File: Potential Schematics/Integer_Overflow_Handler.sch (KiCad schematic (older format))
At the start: 10 parts

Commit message: Made the registers
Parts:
- gave numbers to parts that had none: 7
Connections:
- net CoutALU: now also U35.4; no longer U35.1
- net OP0: now also U10.11; no longer U10.1
- net OP1: now also U10.5; no longer U10.1
- net OP3: now also U10.3; no longer U10.1
- net RS_Latch/R: now also U35.6; no longer U35.3
- net at U21.2: now also U10.4; no longer U10.2
- net at U21.3: now also U21.13; no longer U21.2
- net at U5.1: now also U10.10; no longer U10.2
- net at U5.2: now also U10.6; no longer U10.2
- net at U5.3: now also U21.12; no longer U21.1
- new net: U21.11, U35.5
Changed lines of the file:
@@
 $Descr A4 11693 8268
 encoding utf-8
-Sheet 21 22
+Sheet 21 449
 Title "Integer Overflow Handler"
-Date ""
-Rev ""
+Date "2018-09-14"
+Rev "1"
 Comp ""
 Comment1 ""
@@
 CoutALU
 $Comp
-L 74LS08 U?
+L 74LS08 U21
 U 1 1 5B9D62F2
 P 3600 3400
-F 0 "U?" H 3600 3450 50  0000 C CNN
+F 0 "U21" H 3600 3450 50  0000 C CNN
 F 1 "74LS08" H 3600 3350 50  0000 C CNN
 F 2 "" H 3600 3400 50  0001 C CNN
@@
 $EndComp
 $Comp
-L 74LS08 U?
+L 74LS08 U5
 U 1 1 5B9D634D
 P 3600 2900
-F 0 "U?" H 3600 2950 50  0000 C CNN
+F 0 "U5" H 3600 2950 50  0000 C CNN
 F 1 "74LS08" H 3600 2850 50  0000 C CNN
 F 2 "" H 3600 2900 50  0001 C CNN
@@
 $EndComp
 $Comp
-L 74LS08 U?
-U 1 1 5B9D6375
+L 74LS08 U35
+U 2 1 5B9D6375
 P 6450 3900
-F 0 "U?" H 6450 3950 50  0000 C CNN
+F 0 "U35" H 6450 3950 50  0000 C CNN
 F 1 "74LS08" H 6450 3850 50  0000 C CNN
 F 2 "" H 6450 3900 50  0001 C CNN
 F 3 "" H 6450 3900 50  0001 C CNN
-	1    6450 3900
+	2    6450 3900
 	0    1    1    0
 $EndComp
 $Comp
-L 74LS08 U?
-U 1 1 5B9D643C
+L 74LS08 U21
+U 4 1 5B9D643C
 P 5050 3150
-F 0 "U?" H 5050 3200 50  0000 C CNN
+F 0 "U21" H 5050 3200 50  0000 C CNN
 F 1 "74LS08" H 5050 3100 50  0000 C CNN
 F 2 "" H 5050 3150 50  0001 C CNN
 F 3 "" H 5050 3150 50  0001 C CNN
-	1    5050 3150
+	4    5050 3150
 	1    0    0    -1
 $EndComp
@@
 	2200 3300 3000 3300
 $Comp
-L 74LS04 U?
-U 1 1 5B9D64D7
+L 74LS04 U10
+U 5 1 5B9D64D7
 P 2550 2450
-F 0 "U?" H 2745 2565 50  0000 C CNN
+F 0 "U10" H 2745 2565 50  0000 C CNN
 F 1 "74LS04" H 2740 2325 50  0000 C CNN
 F 2 "" H 2550 2450 50  0001 C CNN
 F 3 "" H 2550 2450 50  0001 C CNN
-	1    2550 2450
+	5    2550 2450
 	1    0    0    -1
 $EndComp
 $Comp
-L 74LS04 U?
-U 1 1 5B9D652D
+L 74LS04 U10
+U 3 1 5B9D652D
 P 2400 2750
-F 0 "U?" H 2595 2865 50  0000 C CNN
+F 0 "U10" H 2595 2865 50  0000 C CNN
 F 1 "74LS04" H 2590 2625 50  0000 C CNN
 F 2 "" H 2400 2750 50  0001 C CNN
 F 3 "" H 2400 2750 50  0001 C CNN
-	1    2400 2750
+	3    2400 2750
 	1    0    0    -1
 $EndComp
 $Comp
-L 74LS04 U?
-U 1 1 5B9D6565
+L 74LS04 U10
+U 2 1 5B9D6565
 P 1950 3400
-F 0 "U?" H 2145 3515 50  0000 C CNN
+F 0 "U10" H 2145 3515 50  0000 C CNN
 F 1 "74LS04" H 2140 3275 50  0000 C CNN
 F 2 "" H 1950 3400 50  0001 C CNN
 F 3 "" H 1950 3400 50  0001 C CNN
-	1    1950 3400
+	2    1950 3400
 	0    1    1    0
 $EndComp
@@
 	1950 2450 2100 2450
 $Comp
-L LED D?
+L LED D1
 U 1 1 5B9D6685
 P 8100 4700
-F 0 "D?" H 8100 4800 50  0000 C CNN
+F 0 "D1" H 8100 4800 50  0000 C CNN
 F 1 "LED" H 8100 4600 50  0000 C CNN
 F 2 "" H 8100 4700 50  0001 C CNN
@@
 $EndComp
 $Comp
-L R R?
+L R R1
 U 1 1 5B9D6786
 P 8400 4700
-F 0 "R?" V 8480 4700 50  0000 C CNN
+F 0 "R1" V 8480 4700 50  0000 C CNN
 F 1 "R" V 8400 4700 50  0000 C CNN
 F 2 "" V 8330 4700 50  0001 C CNN
@@
 $EndComp
 $Comp
-L GND #PWR?
+L GND #PWR1
 U 1 1 5B9D67B7
 P 8550 4700
-F 0 "#PWR?" H 8550 4450 50  0001 C CNN
+F 0 "#PWR1" H 8550 4450 50  0001 C CNN
 F 1 "GND" H 8550 4550 50  0000 C CNN
 F 2 "" H 8550 4700 50  0001 C CNN
@@
 $EndSheet
 $Comp
-L SW_Push SW?
+L SW_Push SW1
 U 1 1 5B9D789D
 P 5150 4700
-F 0 "SW?" H 5200 4800 50  0000 L CNN
+F 0 "SW1" H 5200 4800 50  0000 L CNN
 F 1 "SW_Push" H 5150 4640 50  0000 C CNN
 F 2 "" H 5150 4900 50  0001 C CNN

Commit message: Adding Multiply Devide
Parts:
- D1: symbol LED -> Device:LED
- R1: symbol R -> Device:R
- SW1: symbol SW_Push -> 4-bit_processor-rescue:SW_Push
- U10: symbol 74LS04 -> 4-bit_processor-rescue:74LS04
- U21, U35, U5: symbol 74LS08 -> 4-bit_processor-rescue:74LS08
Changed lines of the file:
@@
-EESchema Schematic File Version 2
-LIBS:power
-LIBS:device
-LIBS:switches
-LIBS:relays
-LIBS:motors
-LIBS:transistors
-LIBS:conn
-LIBS:linear
-LIBS:regul
-LIBS:74xx
-LIBS:cmos4000
-LIBS:adc-dac
-LIBS:memory
-LIBS:xilinx
-LIBS:microcontrollers
-LIBS:dsp
-LIBS:microchip
-LIBS:analog_switches
-LIBS:motorola
-LIBS:texas
-LIBS:intel
-LIBS:audio
-LIBS:interface
-LIBS:digital-audio
-LIBS:philips
-LIBS:display
-LIBS:cypress
-LIBS:siliconi
-LIBS:opto
-LIBS:atmel
-LIBS:contrib
-LIBS:valves
+EESchema Schematic File Version 4
 LIBS:4-bit_processor-cache
-EELAYER 25 0
+EELAYER 26 0
 EELAYER END
 $Descr A4 11693 8268
 encoding utf-8
-Sheet 21 449
+Sheet 21 451
 Title "Integer Overflow Handler"
 Date "2018-09-14"
@@
 CoutALU
 $Comp
-L 74LS08 U21
+L 4-bit_processor-rescue:74LS08 U21
 U 1 1 5B9D62F2
 P 3600 3400
@@
 $EndComp
 $Comp
-L 74LS08 U5
+L 4-bit_processor-rescue:74LS08 U5
 U 1 1 5B9D634D
 P 3600 2900
@@
 $EndComp
 $Comp
-L 74LS08 U35
+L 4-bit_processor-rescue:74LS08 U35
 U 2 1 5B9D6375
 P 6450 3900
@@
 $EndComp
 $Comp
-L 74LS08 U21
+L 4-bit_processor-rescue:74LS08 U21
 U 4 1 5B9D643C
 P 5050 3150
@@
 	2200 3300 3000 3300
 $Comp
-L 74LS04 U10
+L 4-bit_processor-rescue:74LS04 U10
 U 5 1 5B9D64D7
 P 2550 2450
@@
 $EndComp
 $Comp
-L 74LS04 U10
+L 4-bit_processor-rescue:74LS04 U10
 U 3 1 5B9D652D
 P 2400 2750
@@
 $EndComp
 $Comp
-L 74LS04 U10
+L 4-bit_processor-rescue:74LS04 U10
 U 2 1 5B9D6565
 P 1950 3400
@@
 	1950 2450 2100 2450
 $Comp
-L LED D1
+L Device:LED D1
 U 1 1 5B9D6685
 P 8100 4700
@@
 $EndComp
 $Comp
-L R R1
+L Device:R R1
 U 1 1 5B9D6786
 P 8400 4700
@@
 $EndComp
 $Comp
-L GND #PWR1
+L power:GND #PWR1
 U 1 1 5B9D67B7
 P 8550 4700
@@
 $EndSheet
 $Comp
-L SW_Push SW1
+L 4-bit_processor-rescue:SW_Push SW1
 U 1 1 5B9D789D
 P 5150 4700

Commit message: Finished PCB
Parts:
- D1: footprint (none) -> LEDs:LED_D1.8mm_W1.8mm_H2.4mm_Horizontal_O3.81mm_Z4.9mm
- R1: footprint (none) -> Resistors_THT:R_Axial_DIN0922_L20.0mm_D9.0mm_P30.48mm_Horizontal
- SW1: footprint (none) -> Buttons_Switches_THT:SW_DIP_x2_W7.62mm_Slide_LowProfile
- U25: renamed from U10; footprint (none) -> Daniel_Kopp:DIP-14_300_ELL
- U26, U28: renamed from U21; footprint (none) -> Daniel_Kopp:DIP-14_300_ELL
- U26: renamed from U5; footprint (none) -> Daniel_Kopp:DIP-14_300_ELL
- U28: renamed from U35; footprint (none) -> Daniel_Kopp:DIP-14_300_ELL
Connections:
- net OP0: now also U25.9; no longer U25.11
- net OP2: now also U26.12; no longer U26.1
- net at U25.4: now also U26.13; no longer U26.2
- net at U25.6: now also U26.10; no longer U26.2
- net at U28.5: now also U28.3; no longer U28.11
- new net: U26.11, U28.2
- new net: U26.8, U28.1
- new net: U25.8, U26.9
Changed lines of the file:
@@
 $Descr A4 11693 8268
 encoding utf-8
-Sheet 21 451
+Sheet 21 456
 Title "Integer Overflow Handler"
 Date "2018-09-14"
@@
 CoutALU
 $Comp
-L 4-bit_processor-rescue:74LS08 U21
-U 1 1 5B9D62F2
+L 4-bit_processor-rescue:74LS08 U26
+U 4 1 5B9D62F2
 P 3600 3400
-F 0 "U21" H 3600 3450 50  0000 C CNN
+F 0 "U26" H 3600 3450 50  0000 C CNN
 F 1 "74LS08" H 3600 3350 50  0000 C CNN
-F 2 "" H 3600 3400 50  0001 C CNN
+F 2 "Daniel_Kopp:DIP-14_300_ELL" H 3600 3400 50  0001 C CNN
 F 3 "" H 3600 3400 50  0001 C CNN
-	1    3600 3400
+	4    3600 3400
 	1    0    0    -1
 $EndComp
 $Comp
-L 4-bit_processor-rescue:74LS08 U5
-U 1 1 5B9D634D
+L 4-bit_processor-rescue:74LS08 U26
+U 3 1 5B9D634D
 P 3600 2900
-F 0 "U5" H 3600 2950 50  0000 C CNN
+F 0 "U26" H 3600 2950 50  0000 C CNN
 F 1 "74LS08" H 3600 2850 50  0000 C CNN
-F 2 "" H 3600 2900 50  0001 C CNN
+F 2 "Daniel_Kopp:DIP-14_300_ELL" H 3600 2900 50  0001 C CNN
 F 3 "" H 3600 2900 50  0001 C CNN
-	1    3600 2900
+	3    3600 2900
 	1    0    0    -1
 $EndComp
 $Comp
-L 4-bit_processor-rescue:74LS08 U35
+L 4-bit_processor-rescue:74LS08 U28
 U 2 1 5B9D6375
 P 6450 3900
-F 0 "U35" H 6450 3950 50  0000 C CNN
+F 0 "U28" H 6450 3950 50  0000 C CNN
 F 1 "74LS08" H 6450 3850 50  0000 C CNN
-F 2 "" H 6450 3900 50  0001 C CNN
+F 2 "Daniel_Kopp:DIP-14_300_ELL" H 6450 3900 50  0001 C CNN
 F 3 "" H 6450 3900 50  0001 C CNN
 	2    6450 3900
@@
 $EndComp
 $Comp
-L 4-bit_processor-rescue:74LS08 U21
-U 4 1 5B9D643C
+L 4-bit_processor-rescue:74LS08 U28
+U 1 1 5B9D643C
 P 5050 3150
-F 0 "U21" H 5050 3200 50  0000 C CNN
+F 0 "U28" H 5050 3200 50  0000 C CNN
 F 1 "74LS08" H 5050 3100 50  0000 C CNN
-F 2 "" H 5050 3150 50  0001 C CNN
+F 2 "Daniel_Kopp:DIP-14_300_ELL" H 5050 3150 50  0001 C CNN
 F 3 "" H 5050 3150 50  0001 C CNN
-	4    5050 3150
+	1    5050 3150
 	1    0    0    -1
 $EndComp
@@
 	2200 3300 3000 3300
 $Comp
-L 4-bit_processor-rescue:74LS04 U10
-U 5 1 5B9D64D7
+L 4-bit_processor-rescue:74LS04 U25
+U 4 1 5B9D64D7
 P 2550 2450
-F 0 "U10" H 2745 2565 50  0000 C CNN
+F 0 "U25" H 2745 2565 50  0000 C CNN
 F 1 "74LS04" H 2740 2325 50  0000 C CNN
-F 2 "" H 2550 2450 50  0001 C CNN
+F 2 "Daniel_Kopp:DIP-14_300_ELL" H 2550 2450 50  0001 C CNN
 F 3 "" H 2550 2450 50  0001 C CNN
-	5    2550 2450
+	4    2550 2450
 	1    0    0    -1
 $EndComp
 $Comp
-L 4-bit_processor-rescue:74LS04 U10
+L 4-bit_processor-rescue:74LS04 U25
 U 3 1 5B9D652D
 P 2400 2750
-F 0 "U10" H 2595 2865 50  0000 C CNN
+F 0 "U25" H 2595 2865 50  0000 C CNN
 F 1 "74LS04" H 2590 2625 50  0000 C CNN
-F 2 "" H 2400 2750 50  0001 C CNN
+F 2 "Daniel_Kopp:DIP-14_300_ELL" H 2400 2750 50  0001 C CNN
 F 3 "" H 2400 2750 50  0001 C CNN
 	3    2400 2750
@@
 $EndComp
 $Comp
-L 4-bit_processor-rescue:74LS04 U10
+L 4-bit_processor-rescue:74LS04 U25
 U 2 1 5B9D6565
 P 1950 3400
-F 0 "U10" H 2145 3515 50  0000 C CNN
+F 0 "U25" H 2145 3515 50  0000 C CNN
 F 1 "74LS04" H 2140 3275 50  0000 C CNN
-F 2 "" H 1950 3400 50  0001 C CNN
+F 2 "Daniel_Kopp:DIP-14_300_ELL" H 1950 3400 50  0001 C CNN
 F 3 "" H 1950 3400 50  0001 C CNN
 	2    1950 3400
@@
 F 0 "D1" H 8100 4800 50  0000 C CNN
 F 1 "LED" H 8100 4600 50  0000 C CNN
-F 2 "" H 8100 4700 50  0001 C CNN
+F 2 "LEDs:LED_D1.8mm_W1.8mm_H2.4mm_Horizontal_O3.81mm_Z4.9mm" H 8100 4700 50  0001 C CNN
 F 3 "" H 8100 4700 50  0001 C CNN
 	1    8100 4700
@@
 F 0 "R1" V 8480 4700 50  0000 C CNN
 F 1 "R" V 8400 4700 50  0000 C CNN
-F 2 "" V 8330 4700 50  0001 C CNN
+F 2 "Resistors_THT:R_Axial_DIN0922_L20.0mm_D9.0mm_P30.48mm_Horizontal" V 8330 4700 50  0001 C CNN
 F 3 "" H 8400 4700 50  0001 C CNN
 	1    8400 4700
@@
 $EndComp
 $Comp
-L power:GND #PWR1
+L power:GND #PWR01
 U 1 1 5B9D67B7
 P 8550 4700
-F 0 "#PWR1" H 8550 4450 50  0001 C CNN
+F 0 "#PWR01" H 8550 4450 50  0001 C CNN
 F 1 "GND" H 8550 4550 50  0000 C CNN
 F 2 "" H 8550 4700 50  0001 C CNN
@@
 F 0 "SW1" H 5200 4800 50  0000 L CNN
 F 1 "SW_Push" H 5150 4640 50  0000 C CNN
-F 2 "" H 5150 4900 50  0001 C CNN
+F 2 "Buttons_Switches_THT:SW_DIP_x2_W7.62mm_Slide_LowProfile" H 5150 4900 50  0001 C CNN
 F 3 "" H 5150 4900 50  0001 C CNN
 	1    5150 4700

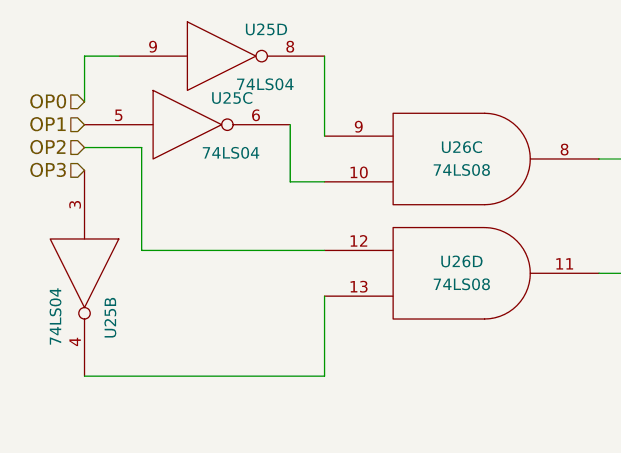
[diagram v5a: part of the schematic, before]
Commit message: Updated overview of Schematic
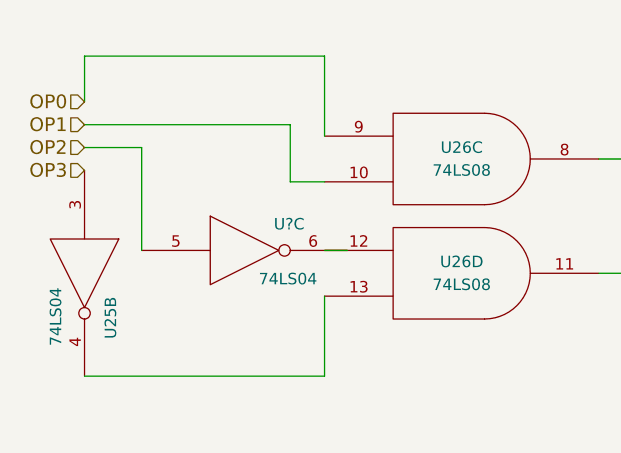
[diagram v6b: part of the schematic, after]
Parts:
- removed unit 4 of U25
- removed unit 3 of U25
- added U?: 74LS04, Daniel_Kopp:DIP-14_300_ELL, symbol 4-bit_processor-rescue:74LS04
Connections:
- net GND: now also U?.7 (GND)
- net OP0: now also U26.9
- net OP1: now also U26.10
- net OP2: now also U?.5; no longer U26.12
- net VCC: now also U?.14 (VCC)
- new net: U26.12, U?.6
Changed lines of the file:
@@
 $Descr A4 11693 8268
 encoding utf-8
-Sheet 21 467
+Sheet 21 902
 Title "Integer Overflow Handler"
 Date "2018-09-14"
@@
 U 4 1 5B9D62F2
 P 3600 3400
+AR Path="/5B9D167A/5B9D5FC6/5B9D62F2" Ref="U26"  Part="4"
+AR Path="/5B9D167A/5BB0D9CD/5B9D62F2" Ref="U302"  Part="3"
 F 0 "U26" H 3600 3450 50  0000 C CNN
 F 1 "74LS08" H 3600 3350 50  0000 C CNN
@@
 U 3 1 5B9D634D
 P 3600 2900
+AR Path="/5B9D167A/5B9D5FC6/5B9D634D" Ref="U26"  Part="3"
+AR Path="/5B9D167A/5BB0D9CD/5B9D634D" Ref="U302"  Part="2"
 F 0 "U26" H 3600 2950 50  0000 C CNN
 F 1 "74LS08" H 3600 2850 50  0000 C CNN
@@
 U 2 1 5B9D6375
 P 6450 3900
+AR Path="/5B9D167A/5B9D5FC6/5B9D6375" Ref="U28"  Part="2"
+AR Path="/5B9D167A/5BB0D9CD/5B9D6375" Ref="U305"  Part="1"
 F 0 "U28" H 6450 3950 50  0000 C CNN
 F 1 "74LS08" H 6450 3850 50  0000 C CNN
@@
 U 1 1 5B9D643C
 P 5050 3150
+AR Path="/5B9D167A/5B9D5FC6/5B9D643C" Ref="U28"  Part="1"
+AR Path="/5B9D167A/5BB0D9CD/5B9D643C" Ref="U302"  Part="4"
 F 0 "U28" H 5050 3200 50  0000 C CNN
 F 1 "74LS08" H 5050 3100 50  0000 C CNN
@@
 Wire Wire Line
 	2200 2850 2200 3300
-Wire Wire Line
-	2200 3300 3000 3300
-$Comp
-L 4-bit_processor-rescue:74LS04 U25
-U 4 1 5B9D64D7
-P 2550 2450
-F 0 "U25" H 2745 2565 50  0000 C CNN
-F 1 "74LS04" H 2740 2325 50  0000 C CNN
-F 2 "Daniel_Kopp:DIP-14_300_ELL" H 2550 2450 50  0001 C CNN
-F 3 "" H 2550 2450 50  0001 C CNN
-	4    2550 2450
-	1    0    0    -1
-$EndComp
-$Comp
-L 4-bit_processor-rescue:74LS04 U25
-U 3 1 5B9D652D
-P 2400 2750
-F 0 "U25" H 2595 2865 50  0000 C CNN
-F 1 "74LS04" H 2590 2625 50  0000 C CNN
-F 2 "Daniel_Kopp:DIP-14_300_ELL" H 2400 2750 50  0001 C CNN
-F 3 "" H 2400 2750 50  0001 C CNN
-	3    2400 2750
-	1    0    0    -1
-$EndComp
 $Comp
 L 4-bit_processor-rescue:74LS04 U25
 U 2 1 5B9D6565
 P 1950 3400
+AR Path="/5B9D167A/5B9D5FC6/5B9D6565" Ref="U25"  Part="2"
+AR Path="/5B9D167A/5BB0D9CD/5B9D6565" Ref="U269"  Part="5"
 F 0 "U25" H 2145 3515 50  0000 C CNN
 F 1 "74LS04" H 2140 3275 50  0000 C CNN
@@
 Wire Wire Line
 	1950 2650 1950 2450
-Wire Wire Line
-	1950 2450 2100 2450
 $Comp
 L Device:LED D1
 U 1 1 5B9D6685
 P 8100 4700
+AR Path="/5B9D167A/5B9D5FC6/5B9D6685" Ref="D1"  Part="1"
+AR Path="/5B9D167A/5BB0D9CD/5B9D6685" Ref="D2"  Part="1"
 F 0 "D1" H 8100 4800 50  0000 C CNN
 F 1 "LED" H 8100 4600 50  0000 C CNN
@@
 U 1 1 5B9D6786
 P 8400 4700
+AR Path="/5B9D167A/5B9D5FC6/5B9D6786" Ref="R1"  Part="1"
+AR Path="/5B9D167A/5BB0D9CD/5B9D6786" Ref="R2"  Part="1"
 F 0 "R1" V 8480 4700 50  0000 C CNN
 F 1 "R" V 8400 4700 50  0000 C CNN
@@
 U 1 1 5B9D67B7
 P 8550 4700
+AR Path="/5B9D167A/5B9D5FC6/5B9D67B7" Ref="#PWR01"  Part="1"
+AR Path="/5B9D167A/5BB0D9CD/5B9D67B7" Ref="#PWR02"  Part="1"
 F 0 "#PWR01" H 8550 4450 50  0001 C CNN
 F 1 "GND" H 8550 4550 50  0000 C CNN
@@
 U 1 1 5B9D789D
 P 5150 4700
+AR Path="/5B9D167A/5B9D5FC6/5B9D789D" Ref="SW1"  Part="1"
+AR Path="/5B9D167A/5BB0D9CD/5B9D789D" Ref="SW2"  Part="1"
 F 0 "SW1" H 5200 4800 50  0000 L CNN
 F 1 "SW_Push" H 5150 4640 50  0000 C CNN
@@
 	7250 4700 7950 4700
 NoConn ~ 7250 4500
+Wire Wire Line
+	1950 2450 3000 2450
+$Comp
+L 4-bit_processor-rescue:74LS04 U?
+U 3 1 5BCC46E6
+P 2650 3300
+AR Path="/5B9D167A/5B9D5FC6/5BCC46E6" Ref="U?"  Part="3"
+AR Path="/5B9D167A/5BB0D9CD/5BCC46E6" Ref="U?"  Part="6"
+F 0 "U?" H 2845 3415 50  0000 C CNN
+F 1 "74LS04" H 2840 3175 50  0000 C CNN
+F 2 "Daniel_Kopp:DIP-14_300_ELL" H 2650 3300 50  0001 C CNN
+F 3 "" H 2650 3300 50  0001 C CNN
+	3    2650 3300
+	1    0    0    -1
+$EndComp
+Wire Wire Line
+	3000 3300 3100 3300
+Wire Wire Line
+	1950 2750 2850 2750
 $EndSCHEMATC
